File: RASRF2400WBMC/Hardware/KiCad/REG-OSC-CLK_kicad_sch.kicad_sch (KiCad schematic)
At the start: 39 parts, among them IC1 ADP7156ACPZ-3.0-R7, IC2 5PB1206NDGK8, J5 1-1478979-0, U2 LD1117DT33TR, Y1 7L-40.000MBS-T

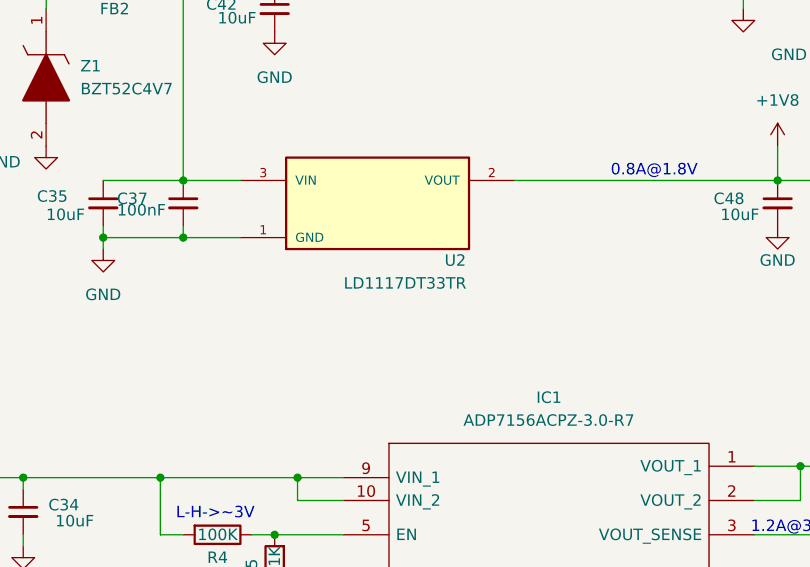
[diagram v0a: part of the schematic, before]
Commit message: Correct the U2 Regulator P/N
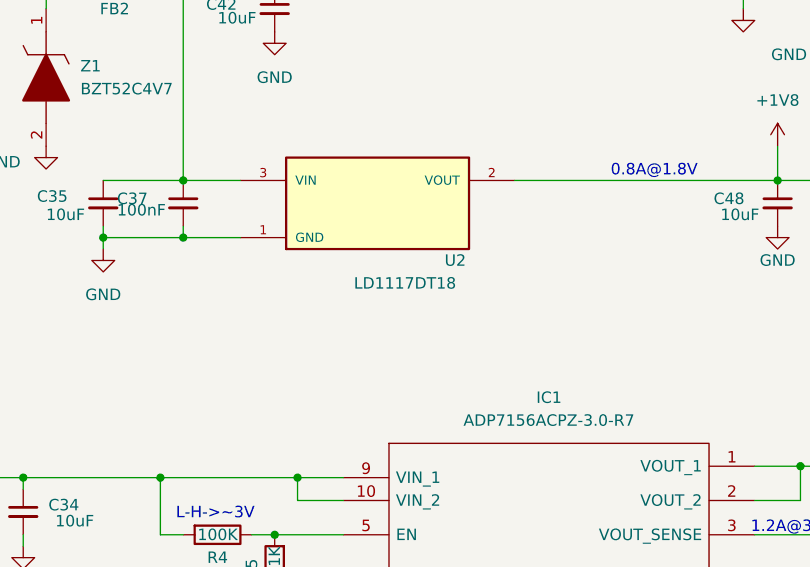
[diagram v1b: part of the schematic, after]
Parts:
- U2: value LD1117DT33TR -> LD1117DT18; Manufacturer_Part_Number LD1117DT33TR -> LD1117DT18CTR, LD1117DT18TR
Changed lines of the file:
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@@
 			)
 		)
-		(property "Value" "LD1117DT33TR"
+		(property "Value" "LD1117DT18"
 			(at 75.438 58.42 0)
 			(effects
@@
 			)
 		)
-		(property "Description" "IC, LDO Regulator, 3.3V, 800mA, Fixed, DPAK (TO-252), T&R"
+		(property "Description" "IC, LDO Regulator, 1.8V, 800mA, Fixed, DPAK (TO-252), T&R"
 			(at 72.39 49.53 0)
 			(effects
@@
 			)
 		)
-		(property "Manufacturer_Part_Number" "LD1117DT33TR"
+		(property "Manufacturer_Part_Number" "LD1117DT18CTR, LD1117DT18TR"
 			(at 72.39 49.53 0)
 			(effects
